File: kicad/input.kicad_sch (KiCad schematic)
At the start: 217 parts, among them J1 IN_1, J2 IN_2, Q1 CSD13380F3, Q5 CSD13380F3, SW1 RotaryEncoder, SW10 DG1411EEQ, SW11 DG1413EEQ, SW2 INST_IND_1, SW3 DG1413EEQ, SW4 DG1411EEQ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

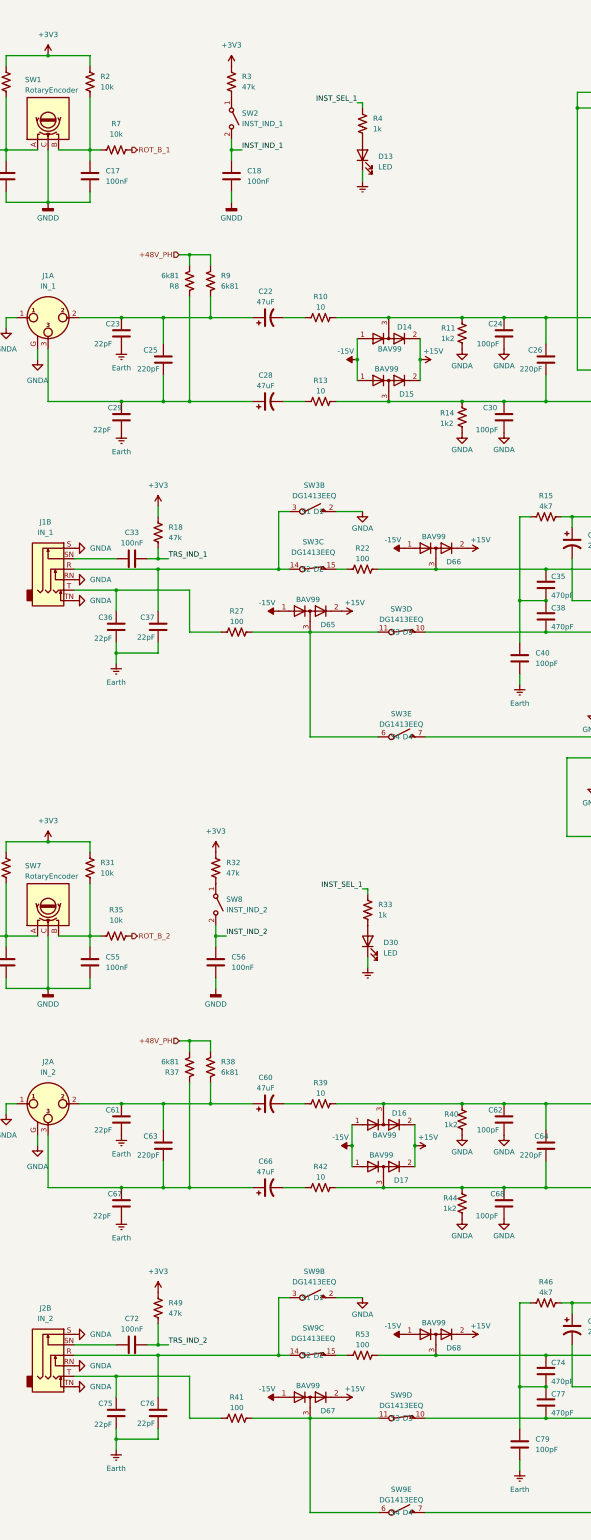
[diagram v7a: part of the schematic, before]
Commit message: push buttons
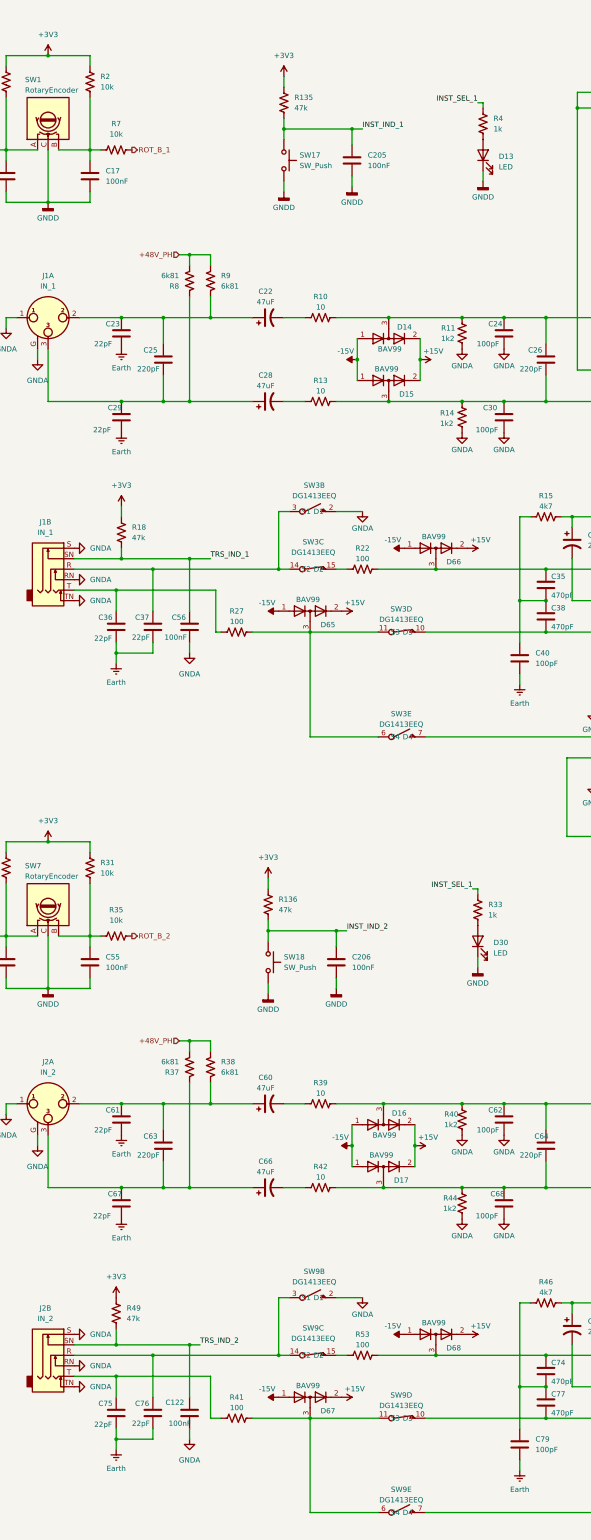
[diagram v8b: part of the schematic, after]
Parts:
- removed C18, C33, C72: 100nF, symbol Device:C
- removed R3, R32: 47k, symbol Device:R_US
- removed SW2: INST_IND_1, symbol Switch:SW_SPST
- removed SW8: INST_IND_2, symbol Switch:SW_SPST
- added C122: 100nF, symbol Device:C
- added C205, C206: 100nF, Capacitor_SMD:C_0603_1608Metric_Pad1.08x0.95mm_HandSolder, symbol Device:C
- added R135, R136: 47k, Resistor_SMD:R_0603_1608Metric_Pad0.98x0.95mm_HandSolder, symbol Device:R_US
- added SW17, SW18: SW_Push, Button_Switch_SMD:SW_Push_1P1T_XKB_TS-1187A, symbol Switch:SW_Push
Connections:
- net +3V3: now also R135.1, R136.1
- net Earth: no longer D13.1 (K), D30.1 (K)
- net GNDA: now also C56.2, C122.2
- net GNDD: now also D13.1 (K), D30.1 (K), C205.2, C206.2, SW17.2, SW18.2; no longer C56.2
- net INST_IND_1: now also C205.1, R135.2, SW17.1
- net INST_IND_2: now also C206.1, R136.2, SW18.1; no longer C56.1
- net TRS_IND_1: now also C56.1, J1.SN
- net TRS_IND_2: now also J2.SN, C122.1
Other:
- moved on the sheet: C37, C76, D13, D30, R18, R33, R4, R49
